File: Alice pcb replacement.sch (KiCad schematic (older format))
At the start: 14 parts

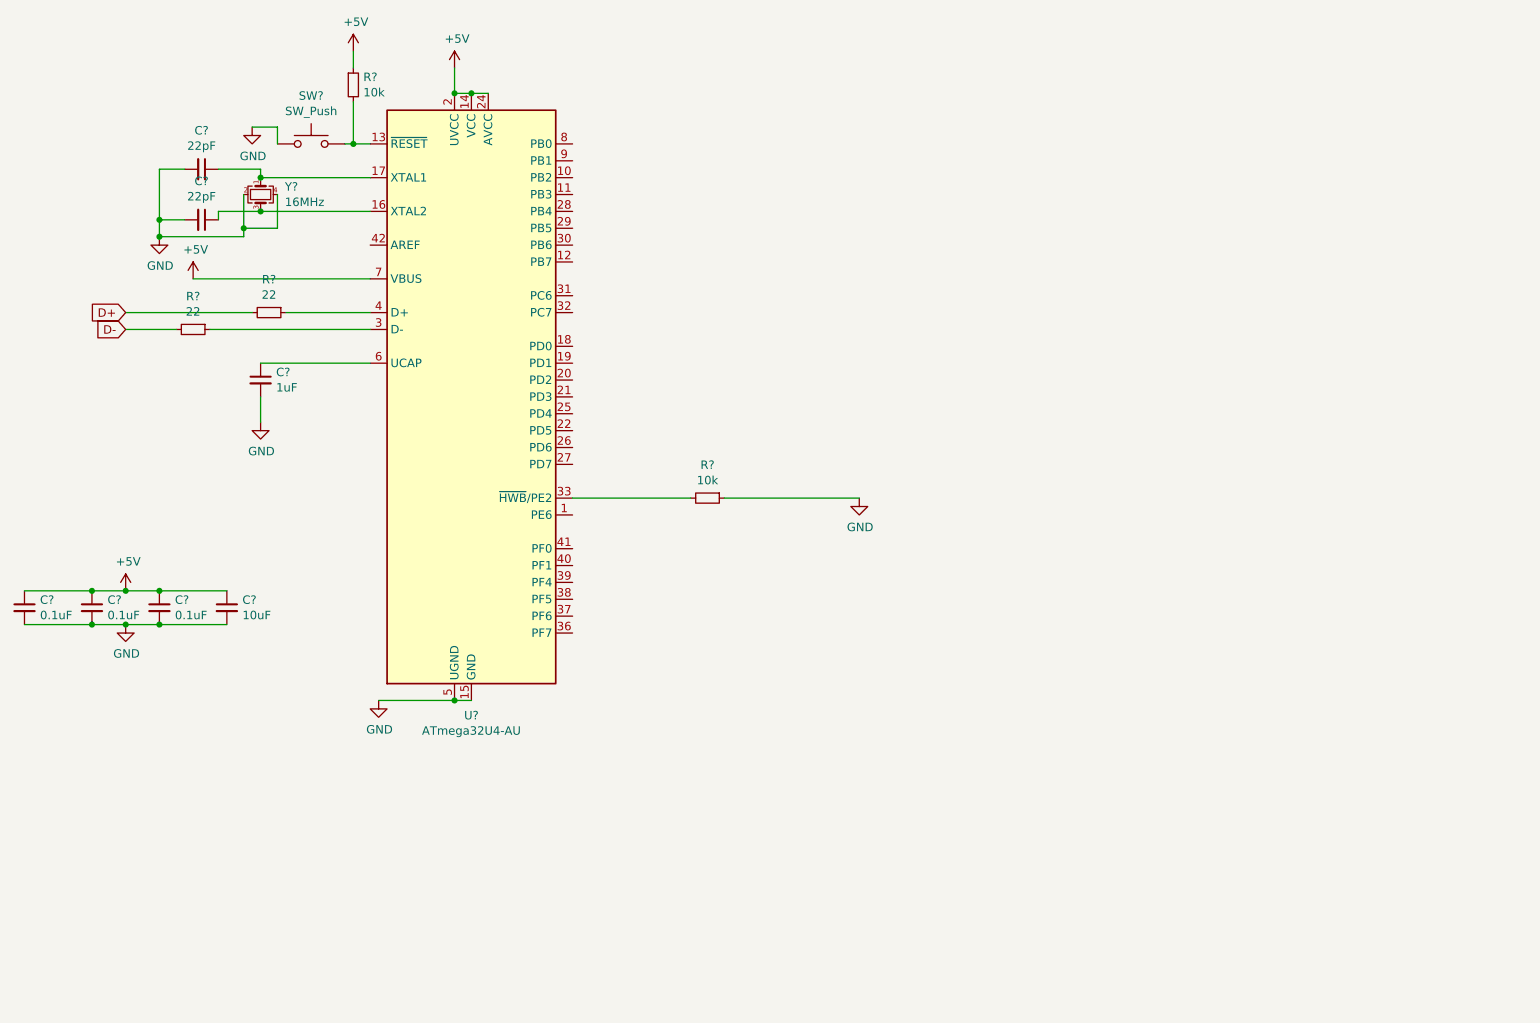
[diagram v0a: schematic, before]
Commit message: Add submodules
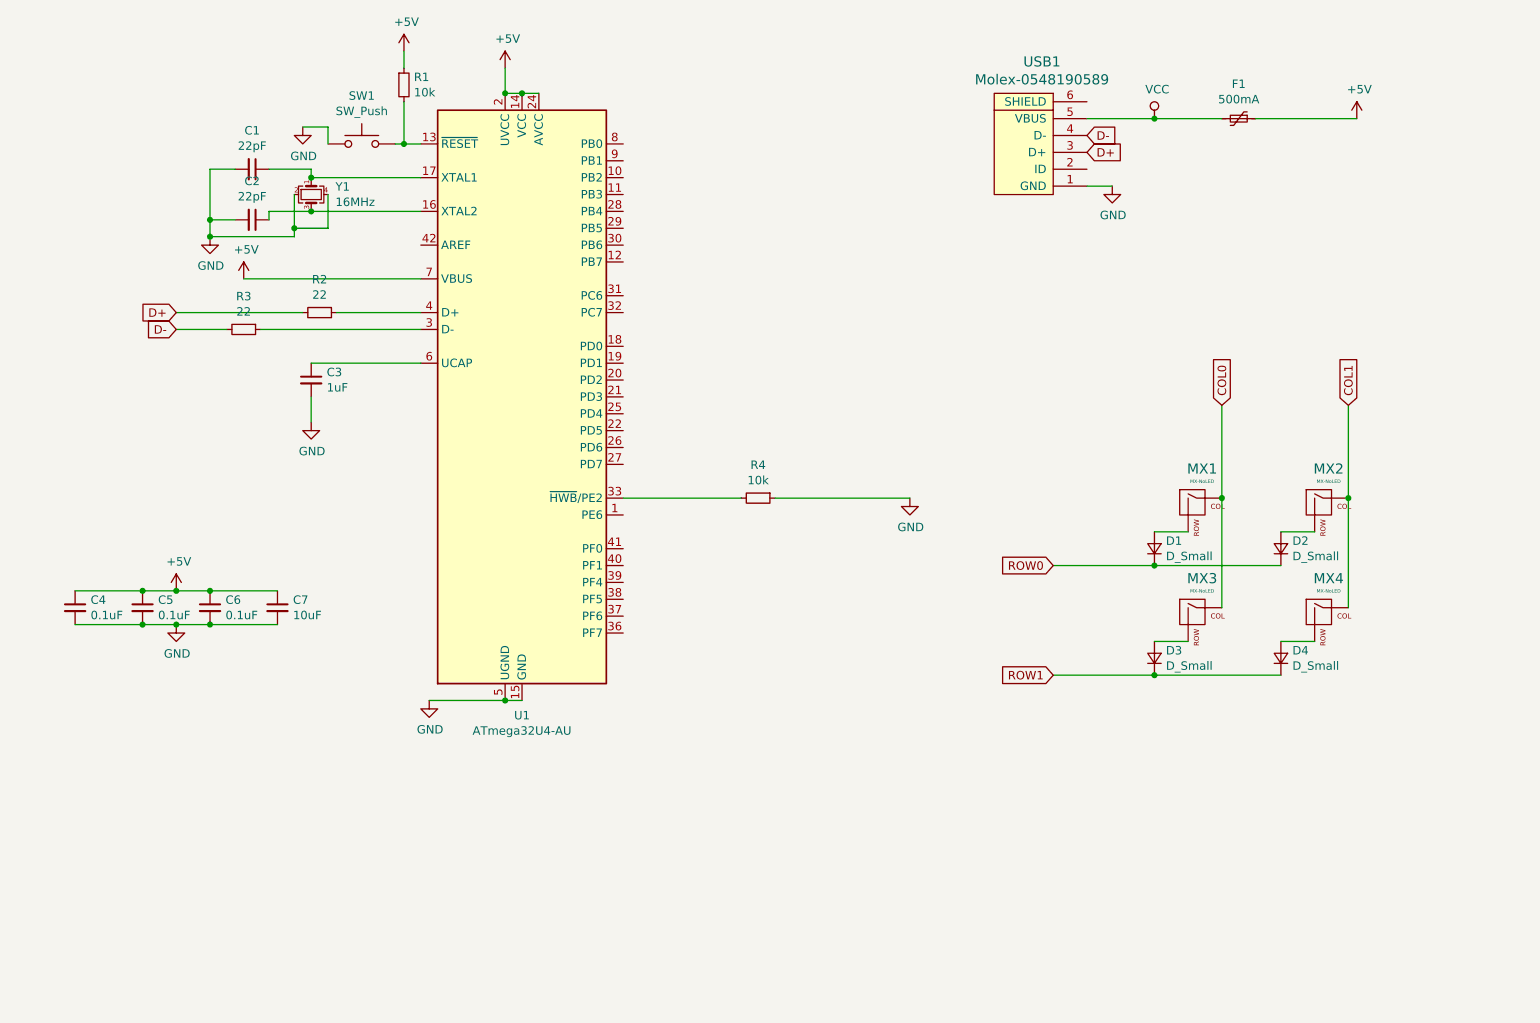
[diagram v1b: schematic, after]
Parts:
- added D1, D2, D3, D4: D_Small, symbol Device:D_Small
- added F1: 500mA, symbol Device:Polyfuse_Small
- added MX1, MX2, MX3, MX4: MX-NoLED, symbol MX_Alps_Hybrid:MX-NoLED
- added USB1: Molex-0548190589, symbol random-keyboard-parts:Molex-0548190589
- gave numbers to parts that had none: 14
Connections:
- net +5V: now also F1.1
- net D+: now also USB1.3 (D+)
- net D-: now also USB1.4 (D-)
- net GND: now also USB1.1 (GND)
- new net: D1.2 (A), MX1.2 (ROW)
- new net: D2.2 (A), MX2.2 (ROW)
- new net: D3.2 (A), MX3.2 (ROW)
- new net: D4.2 (A), MX4.2 (ROW)
- new net COL0: MX1.1 (COL), MX3.1 (COL)
- new net COL1: MX2.1 (COL), MX4.1 (COL)
- new net ROW0: D1.1 (K), D2.1 (K)
- new net ROW1: D3.1 (K), D4.1 (K)
- new net VCC: F1.2, USB1.5 (VBUS)
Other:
- moved on the sheet: C1, C2, C3, C4, C5, C6, C7, R1, R2, R3, R4, SW1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

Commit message: Done assigning footprints
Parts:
- C1, C2, C3, C4, C5, C6, C7: footprint (none) -> Capacitor_SMD:C_0805_2012Metric
- D1, D2, D3, D4: footprint (none) -> Diode_SMD:D_SOD-123
- F1: footprint (none) -> Fuse:Fuse_1206_3216Metric
- MX1, MX2, MX3, MX4: footprint (none) -> MX_Alps_Hybrid:MX-1U
- R1, R2, R3, R4: footprint (none) -> Resistor_SMD:R_0805_2012Metric
- SW1: footprint (none) -> random-keyboard-parts:SKQG-1155865
- USB1: footprint (none) -> random-keyboard-parts:Molex-0548190589
- Y1: footprint (none) -> Crystal:Crystal_SMD_3225-4Pin_3.2x2.5mm

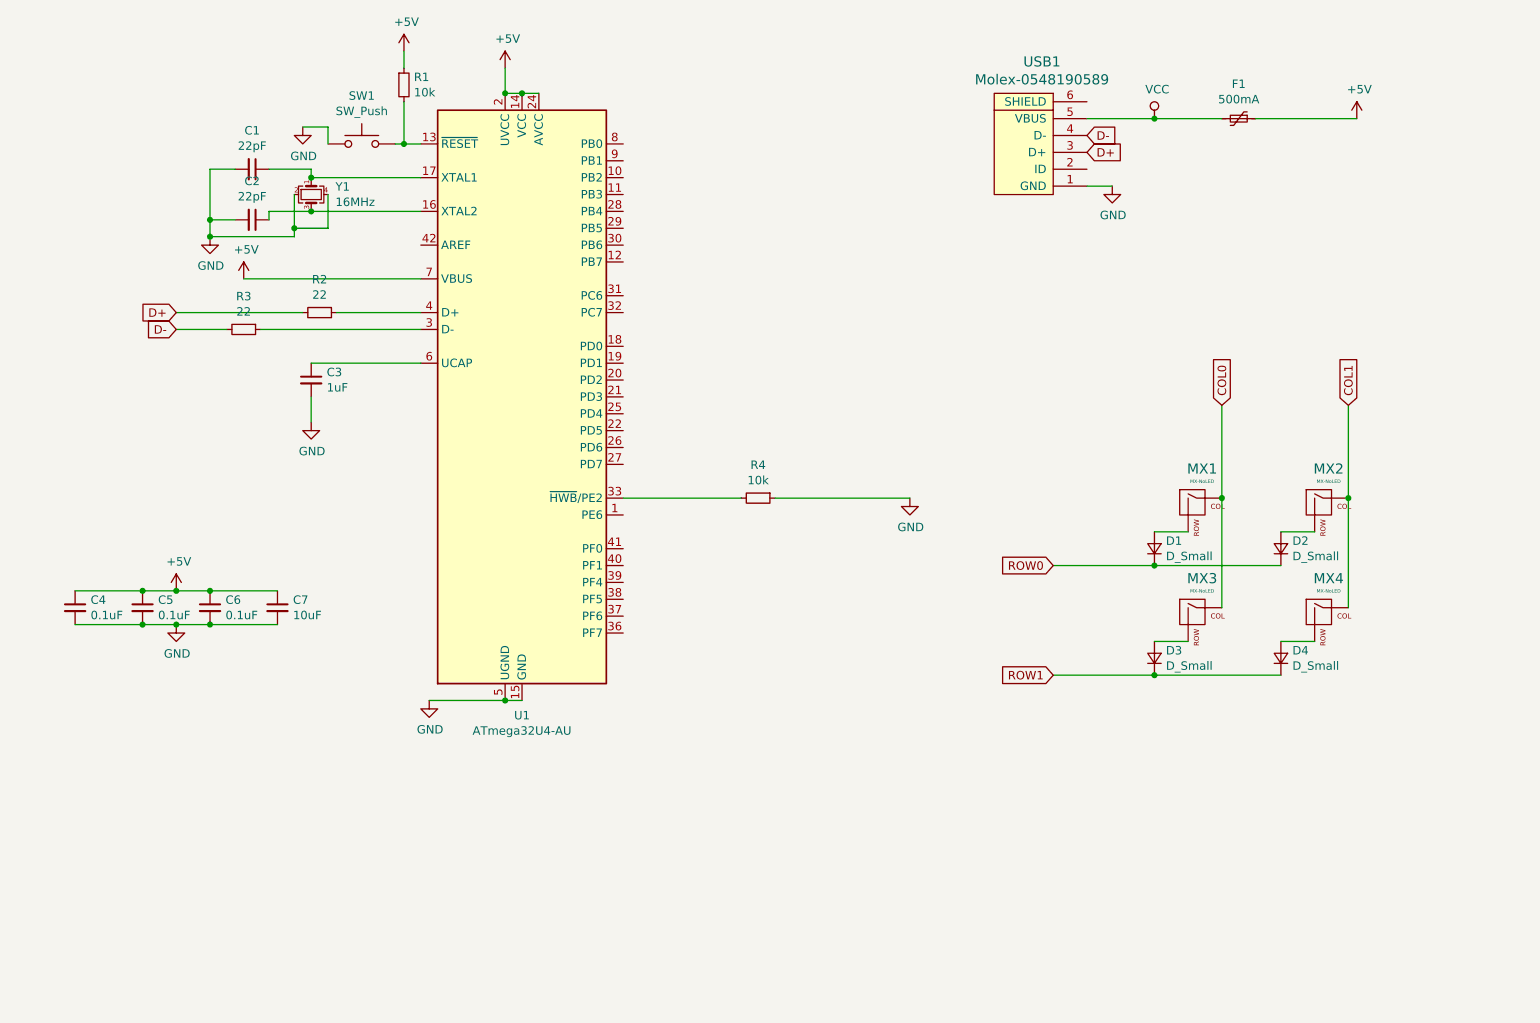
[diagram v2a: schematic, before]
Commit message: Moved Components to PCB area
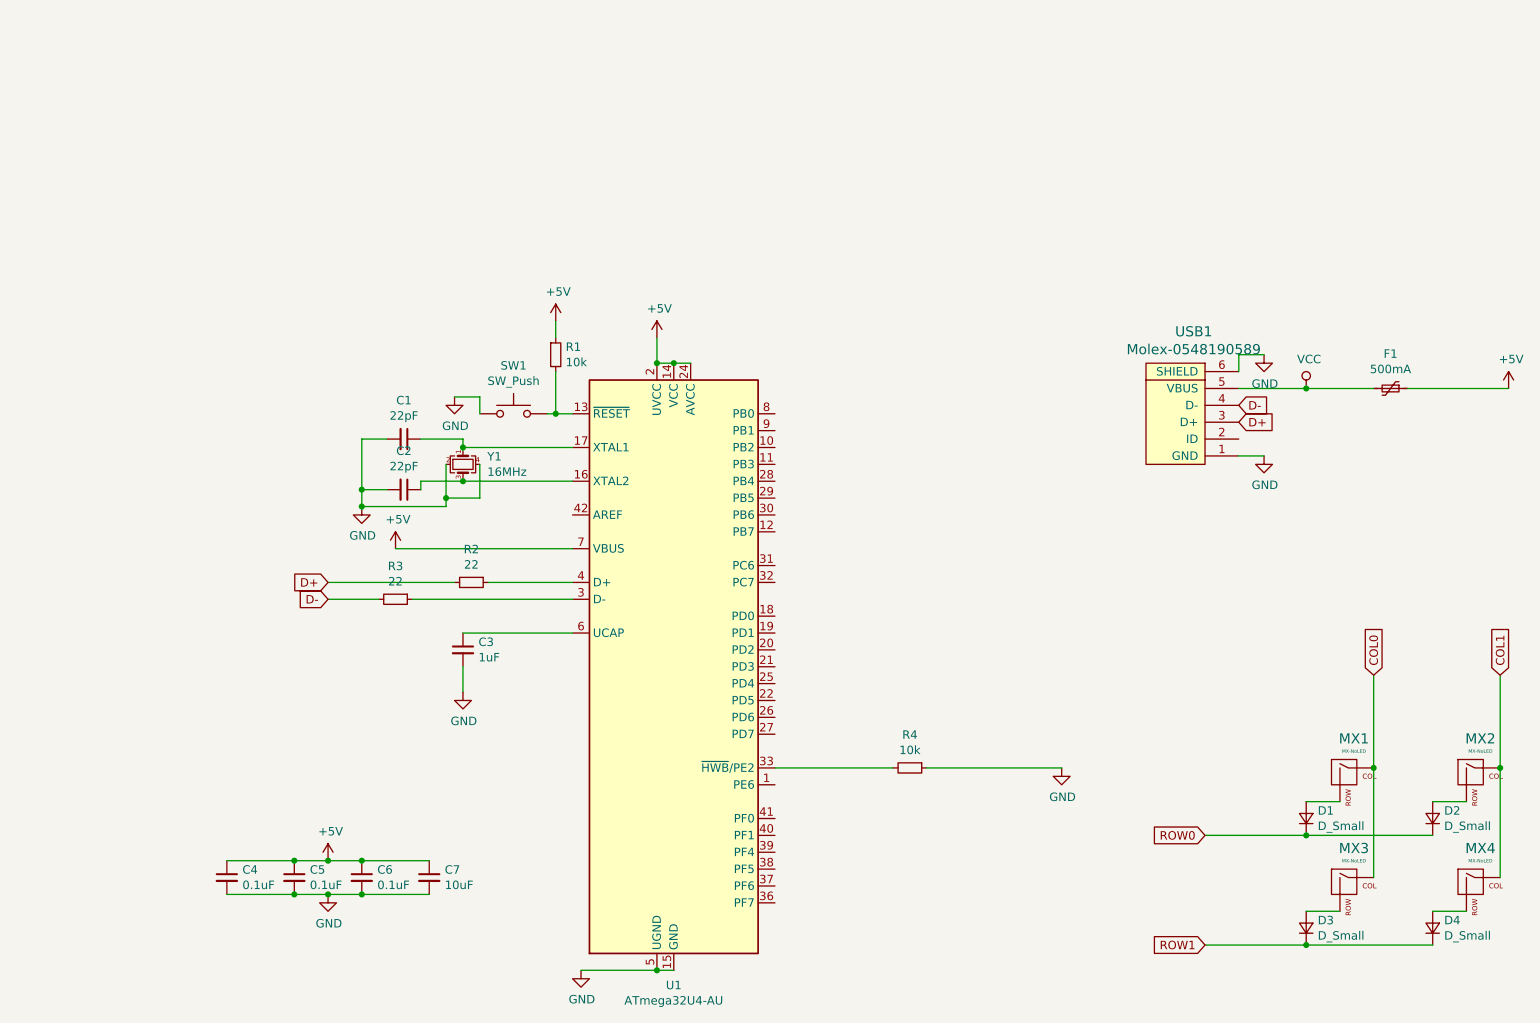
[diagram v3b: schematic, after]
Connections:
- net GND: now also USB1.6 (SHIELD)
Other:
- moved on the sheet: C1, C2, C3, C4, C5, C6, C7, D1, D2, D3, D4, F1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
